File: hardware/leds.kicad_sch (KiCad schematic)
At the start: 83 parts

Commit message: :construction: some chip layout
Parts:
- LED1, LED10, LED11, LED12, LED13, LED14, LED15, LED16, LED17, LED18, LED19, LED2, LED20, LED21, LED22, LED23, LED24, LED25, LED26, LED27, LED28, LED29, LED3, LED30, LED31, LED32, LED33, LED34, LED35, LED36, LED37, LED38, LED39, LED4, LED40, LED41, LED42, LED43, LED44, LED45, LED46, LED47, LED48, LED49, LED5, LED50, LED51, LED52, LED53, LED54, LED55, LED56, LED57, LED58, LED59, LED6, LED60, LED61, LED62, LED63, LED64, LED65, LED66, LED67, LED68, LED69, LED7, LED70, LED71, LED72, LED73, LED74, LED75, LED76, LED77, LED78, LED79, LED8, LED80, LED81, LED82, LED9: symbol components:XL-6028RGBW-WS2812B -> KeysDock:XL-6028RGBW-WS2812B

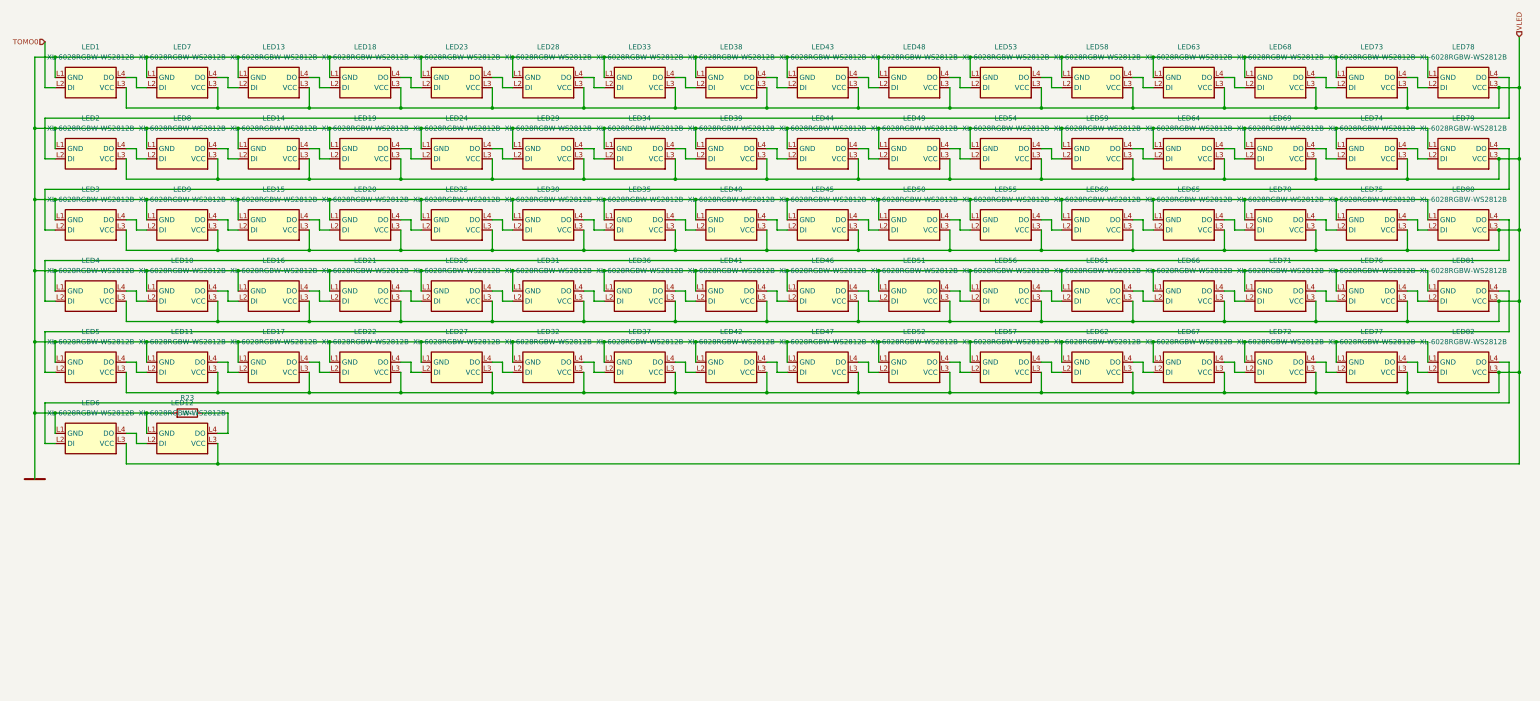
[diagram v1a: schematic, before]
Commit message: :construction: awake and sleep lines
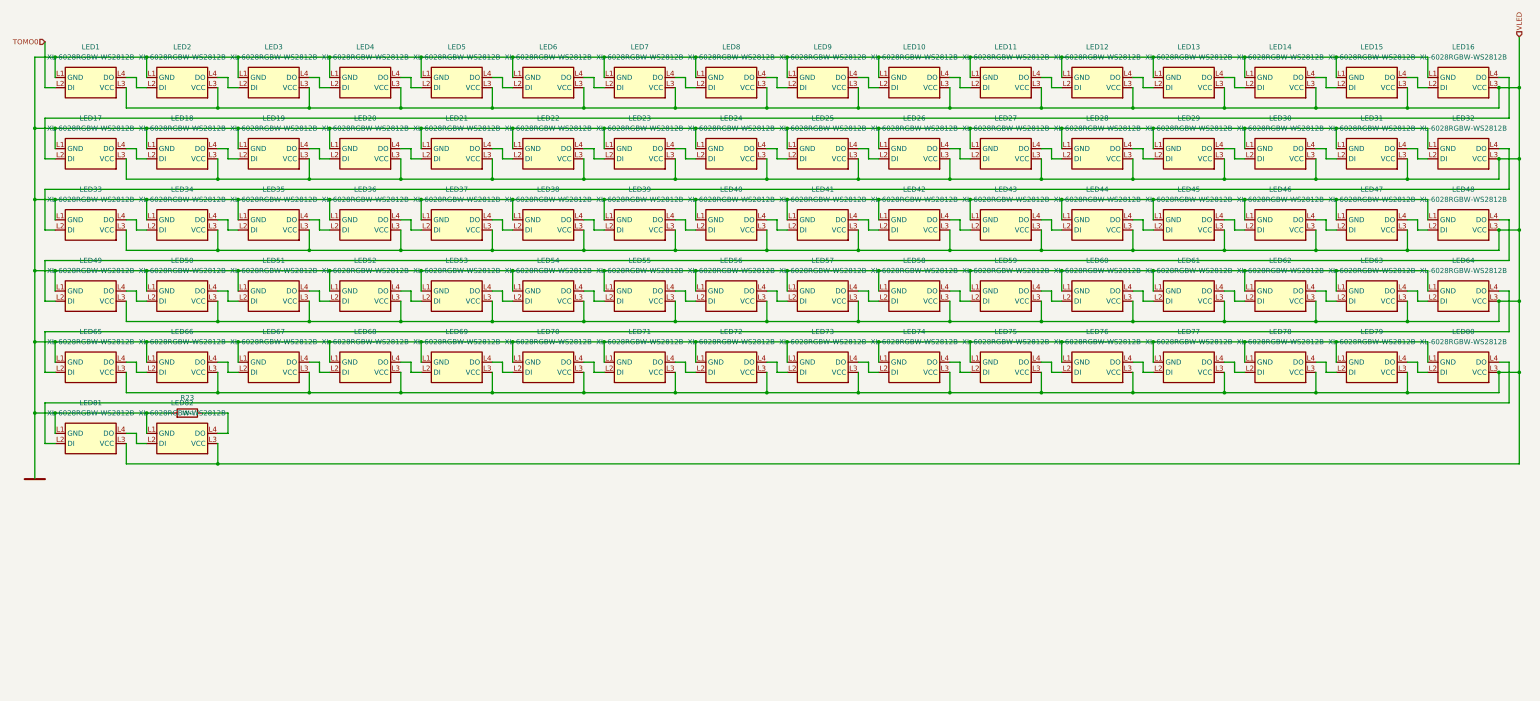
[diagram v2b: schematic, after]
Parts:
- renumbered LED48 to LED10, LED53 to LED11, LED58 to LED12, LED63 to LED13, LED68 to LED14, LED73 to LED15, LED78 to LED16, LED2 to LED17, LED8 to LED18, LED14 to LED19, LED7 to LED2, LED19 to LED20, LED24 to LED21, LED29 to LED22, LED34 to LED23, LED39 to LED24, LED44 to LED25, LED49 to LED26, LED54 to LED27, LED59 to LED28, LED64 to LED29, LED13 to LED3, LED69 to LED30, LED74 to LED31, LED79 to LED32, LED3 to LED33, LED9 to LED34, LED15 to LED35, LED20 to LED36, LED25 to LED37, LED30 to LED38, LED35 to LED39, LED18 to LED4, LED45 to LED41, LED50 to LED42, LED55 to LED43, LED60 to LED44, LED65 to LED45, LED70 to LED46, LED75 to LED47, LED80 to LED48, LED4 to LED49, LED23 to LED5, LED10 to LED50, LED16 to LED51, LED21 to LED52, LED26 to LED53, LED31 to LED54, LED36 to LED55, LED41 to LED56, LED46 to LED57, LED51 to LED58, LED56 to LED59, LED28 to LED6, LED61 to LED60, LED66 to LED61, LED71 to LED62, LED76 to LED63, LED81 to LED64, LED5 to LED65, LED11 to LED66, LED17 to LED67, LED22 to LED68, LED27 to LED69, LED33 to LED7, LED32 to LED70, LED37 to LED71, LED42 to LED72, LED47 to LED73, LED52 to LED74, LED57 to LED75, LED62 to LED76, LED67 to LED77, LED72 to LED78, LED77 to LED79, LED38 to LED8, LED82 to LED80, LED6 to LED81, LED12 to LED82, LED43 to LED9
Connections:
- net P,E renamed P,0

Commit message: :sparkles: use net tie to construct GNDs
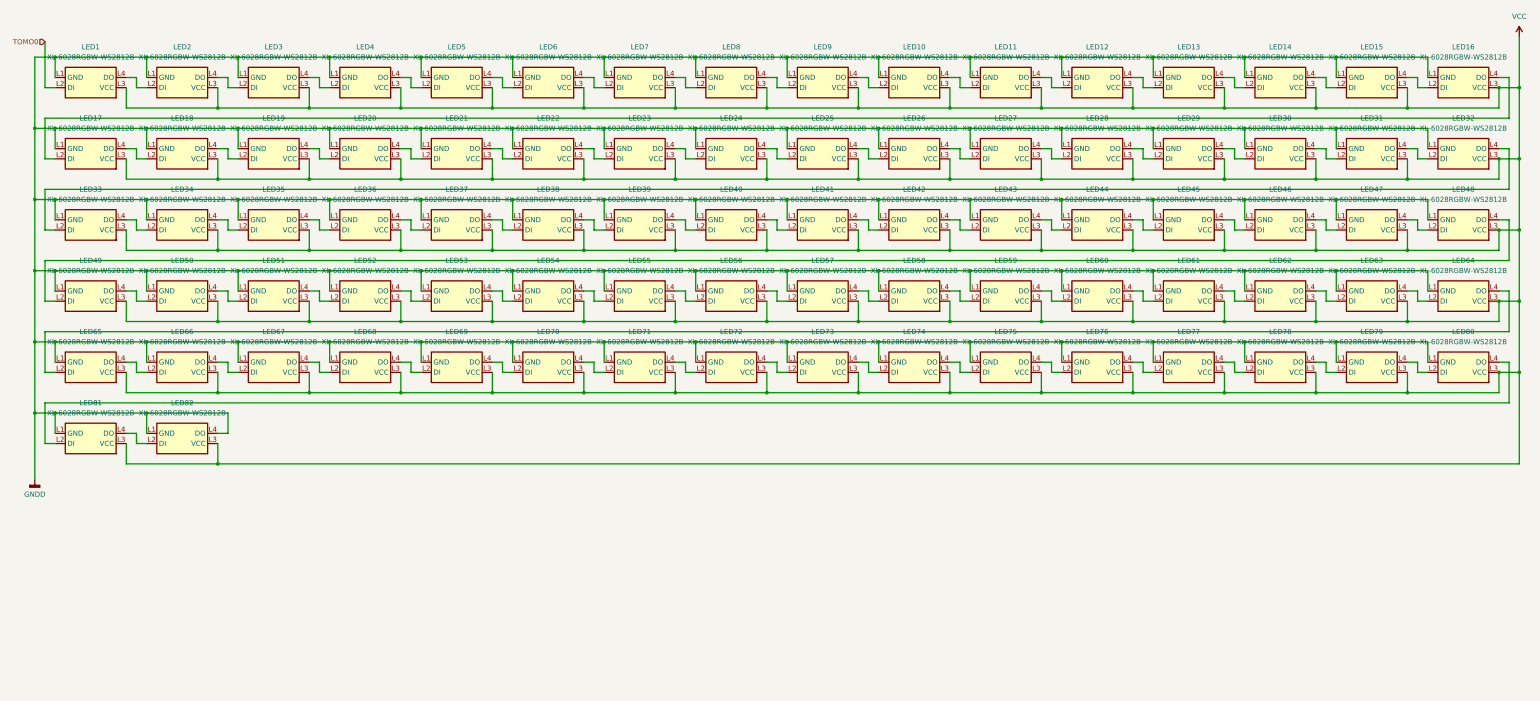
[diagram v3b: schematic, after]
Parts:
- removed R23: 100Ω, KeysDock:R_0402, symbol KeysDock:0402,100Ω
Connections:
- net P,0 is gone; now on net GNDD: LED1.L1 (GND), LED10.L1 (GND), LED11.L1 (GND), LED12.L1 (GND), LED13.L1 (GND), LED14.L1 (GND), LED15.L1 (GND), LED16.L1 (GND), LED17.L1 (GND), LED18.L1 (GND), LED19.L1 (GND), LED2.L1 (GND), LED20.L1 (GND), LED21.L1 (GND), LED22.L1 (GND), LED23.L1 (GND), LED24.L1 (GND), LED25.L1 (GND), LED26.L1 (GND), LED27.L1 (GND), LED28.L1 (GND), LED29.L1 (GND), LED3.L1 (GND), LED30.L1 (GND), LED31.L1 (GND), LED32.L1 (GND), LED33.L1 (GND), LED34.L1 (GND), LED35.L1 (GND), LED36.L1 (GND), LED37.L1 (GND), LED38.L1 (GND), LED39.L1 (GND), LED4.L1 (GND), LED40.L1 (GND), LED41.L1 (GND), LED42.L1 (GND), LED43.L1 (GND), LED44.L1 (GND), LED45.L1 (GND), LED46.L1 (GND), LED47.L1 (GND), LED48.L1 (GND), LED49.L1 (GND), LED5.L1 (GND), LED50.L1 (GND), LED51.L1 (GND), LED52.L1 (GND), LED53.L1 (GND), LED54.L1 (GND), LED55.L1 (GND), LED56.L1 (GND), LED57.L1 (GND), LED58.L1 (GND), LED59.L1 (GND), LED6.L1 (GND), LED60.L1 (GND), LED61.L1 (GND), LED62.L1 (GND), LED63.L1 (GND), LED64.L1 (GND), LED65.L1 (GND), LED66.L1 (GND), LED67.L1 (GND), LED68.L1 (GND), LED69.L1 (GND), LED7.L1 (GND), LED70.L1 (GND), LED71.L1 (GND), LED72.L1 (GND), LED73.L1 (GND), LED74.L1 (GND), LED75.L1 (GND), LED76.L1 (GND), LED77.L1 (GND), LED78.L1 (GND), LED79.L1 (GND), LED8.L1 (GND), LED80.L1 (GND), LED81.L1 (GND), LED82.L1 (GND), LED9.L1 (GND)
- net GNDD: now reaches LED82.L4 (DO)
- net VLED renamed VCC

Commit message: :sparkles: add capacitor for LEDs
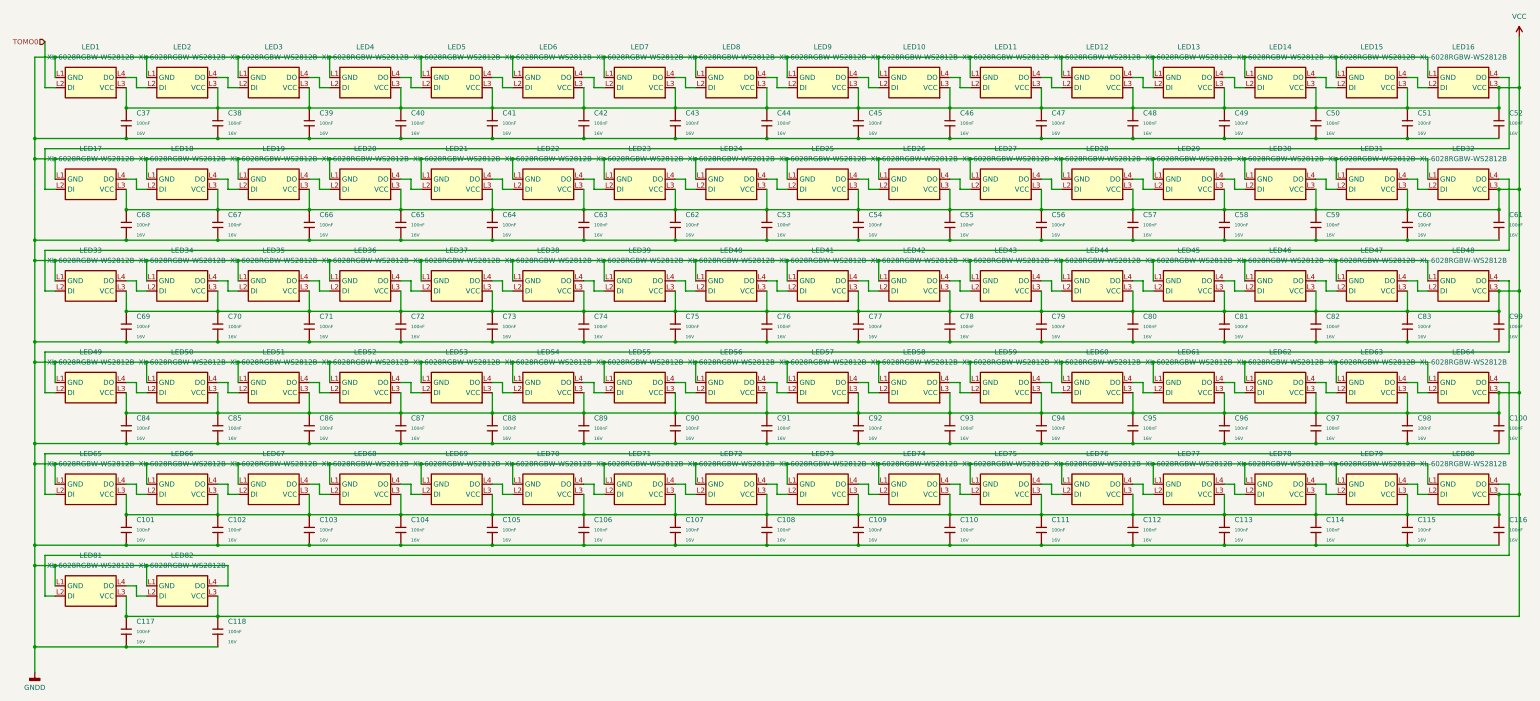
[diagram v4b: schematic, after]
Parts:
- added C100, C101, C102, C103, C104, C105, C106, C107, C108, C109, C110, C111, C112, C113, C114, C115, C116, C117, C118, C37, C38, C39, C40, C41, C42, C43, C44, C45, C46, C47, C48, C49, C50, C51, C52, C53, C54, C55, C56, C57, C58, C59, C60, C61, C62, C63, C64, C65, C66, C67, C68, C69, C70, C71, C72, C73, C74, C75, C76, C77, C78, C79, C80, C81, C82, C83, C84, C85, C86, C87, C88, C89, C90, C91, C92, C93, C94, C95, C96, C97, C98, C99: 100nF, KeysDock:C_0402, symbol KeysDock:0402,100nF
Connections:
- net GNDD: now also C100.2, C101.2, C102.2, C103.2, C104.2, C105.2, C106.2, C107.2, C108.2, C109.2, C110.2, C111.2, C112.2, C113.2, C114.2, C115.2, C116.2, C117.2, C118.2, C37.2, C38.2, C39.2, C40.2, C41.2, C42.2, C43.2, C44.2, C45.2, C46.2, C47.2, C48.2, C49.2, C50.2, C51.2, C52.2, C53.2, C54.2, C55.2, C56.2, C57.2, C58.2, C59.2, C60.2, C61.2, C62.2, C63.2, C64.2, C65.2, C66.2, C67.2, C68.2, C69.2, C70.2, C71.2, C72.2, C73.2, C74.2, C75.2, C76.2, C77.2, C78.2, C79.2, C80.2, C81.2, C82.2, C83.2, C84.2, C85.2, C86.2, C87.2, C88.2, C89.2, C90.2, C91.2, C92.2, C93.2, C94.2, C95.2, C96.2, C97.2, C98.2, C99.2
- net VCC: now also C100.1, C101.1, C102.1, C103.1, C104.1, C105.1, C106.1, C107.1, C108.1, C109.1, C110.1, C111.1, C112.1, C113.1, C114.1, C115.1, C116.1, C117.1, C118.1, C37.1, C38.1, C39.1, C40.1, C41.1, C42.1, C43.1, C44.1, C45.1, C46.1, C47.1, C48.1, C49.1, C50.1, C51.1, C52.1, C53.1, C54.1, C55.1, C56.1, C57.1, C58.1, C59.1, C60.1, C61.1, C62.1, C63.1, C64.1, C65.1, C66.1, C67.1, C68.1, C69.1, C70.1, C71.1, C72.1, C73.1, C74.1, C75.1, C76.1, C77.1, C78.1, C79.1, C80.1, C81.1, C82.1, C83.1, C84.1, C85.1, C86.1, C87.1, C88.1, C89.1, C90.1, C91.1, C92.1, C93.1, C94.1, C95.1, C96.1, C97.1, C98.1, C99.1
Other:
- moved on the sheet: LED17, LED18, LED19, LED20, LED21, LED22, LED23, LED24, LED25, LED26, LED27, LED28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
